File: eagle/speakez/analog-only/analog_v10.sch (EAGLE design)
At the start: 46 parts, among them U1 +12v, U2 MAX5486

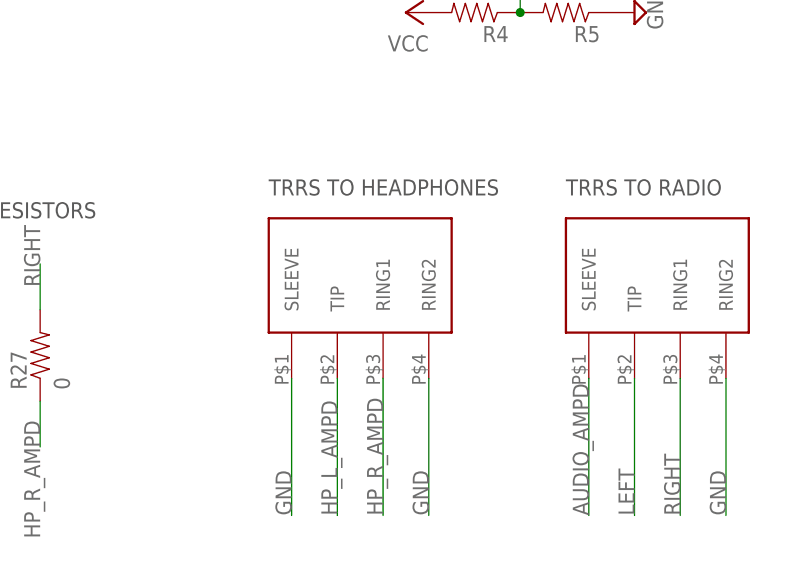
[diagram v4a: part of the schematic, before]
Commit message: got rid of mute + headphone jack; added solder holes + strain relief
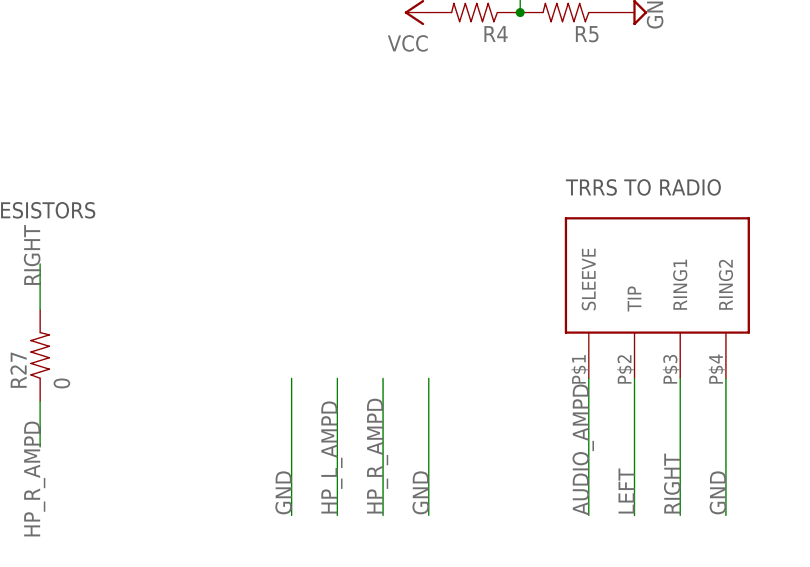
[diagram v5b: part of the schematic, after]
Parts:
- removed HP: SJ-43514-SMT, 35mm_audio:SJ-43514-SMT
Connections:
- net GND: no longer HP.RING2, HP.SLEEVE
- net HP_L_AMPD: no longer HP.TIP
- net HP_R_AMPD: no longer HP.RING1
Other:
- note removed: "TRRS TO HEADPHONES"
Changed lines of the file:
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@@
 <?xml version="1.0" encoding="utf-8"?>
 <!DOCTYPE eagle SYSTEM "eagle.dtd">
-<eagle version="7.6.0">
+<eagle version="7.7.0">
 <drawing>
 <settings>
@@
 <part name="C9" library="SparkFun-Passives" deviceset="CAP" device="0805" value="0.1 uF"/>
 <part name="P+5" library="supply1" deviceset="VCC" device=""/>
-<part name="HP" library="35mm_audio" deviceset="SJ-43514-SMT" device=""/>
 <part name="RADIO" library="35mm_audio" deviceset="SJ-43514-SMT" device=""/>
 <part name="VD2" library="diode" deviceset="DIODE-SCHOTTKY-" device="SOD123" value="40V AF DIODE"/>
@@
 <sheet>
 <plain>
-<text x="50.8" y="15.24" size="1.778" layer="97">TRRS TO HEADPHONES</text>
 <text x="83.82" y="15.24" size="1.778" layer="97">TRRS TO RADIO</text>
 <text x="10.16" y="12.7" size="1.778" layer="97">BYPASS RESISTORS</text>
@@
 <instance part="C9" gate="G$1" x="71.12" y="114.3"/>
 <instance part="P+5" gate="VCC" x="78.74" y="119.38" rot="R270"/>
-<instance part="HP" gate="G$1" x="53.34" y="0"/>
 <instance part="RADIO" gate="G$1" x="86.36" y="0"/>
 <instance part="VD2" gate="G$1" x="50.8" y="119.38"/>
@@
 </segment>
 <segment>
-<pinref part="HP" gate="G$1" pin="RING1"/>
 <wire x1="63.5" y1="-5.08" x2="63.5" y2="-20.32" width="0.1524" layer="91"/>
 <label x="63.5" y="-20.32" size="1.778" layer="95" rot="R90"/>
@@
 </segment>
 <segment>
-<pinref part="HP" gate="G$1" pin="TIP"/>
 <wire x1="58.42" y1="-5.08" x2="58.42" y2="-20.32" width="0.1524" layer="91"/>
 <label x="58.42" y="-20.32" size="1.778" layer="95" rot="R90"/>
@@
 <net name="GND" class="0">
 <segment>
-<pinref part="HP" gate="G$1" pin="SLEEVE"/>
 <wire x1="53.34" y1="-5.08" x2="53.34" y2="-20.32" width="0.1524" layer="91"/>
 <label x="53.34" y="-20.32" size="1.778" layer="95" rot="R90"/>
@@
 </segment>
 <segment>
-<pinref part="HP" gate="G$1" pin="RING2"/>
 <wire x1="68.58" y1="-5.08" x2="68.58" y2="-20.32" width="0.1524" layer="91"/>
 <label x="68.58" y="-20.32" size="1.778" layer="95" rot="R90"/>

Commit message: final tweaks
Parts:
- R9: value 100M -> 1M
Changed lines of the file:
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@@
 <?xml version="1.0" encoding="utf-8"?>
 <!DOCTYPE eagle SYSTEM "eagle.dtd">
-<eagle version="7.7.0">
+<eagle version="7.6.0">
 <drawing>
 <settings>
@@
 <part name="C11" library="SparkFun-Passives" deviceset="CAP" device="0805" value="100pF"/>
 <part name="SUPPLY15" library="supply2" deviceset="GND" device=""/>
-<part name="R9" library="SparkFun-Passives" deviceset="RESISTOR" device="0805-RES" value="100M"/>
+<part name="R9" library="SparkFun-Passives" deviceset="RESISTOR" device="0805-RES" value="1M"/>
 <part name="R10" library="SparkFun-Passives" deviceset="RESISTOR" device="0805-RES" value="330"/>
 <part name="R11" library="SparkFun-Passives" deviceset="RESISTOR" device="0805-RES" value="330"/>
